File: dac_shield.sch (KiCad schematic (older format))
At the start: 26 parts, among them P1 V+, P2 GND, P3 V-, P4 Out, P5 GND, U1 LM741, U2 TCA0372

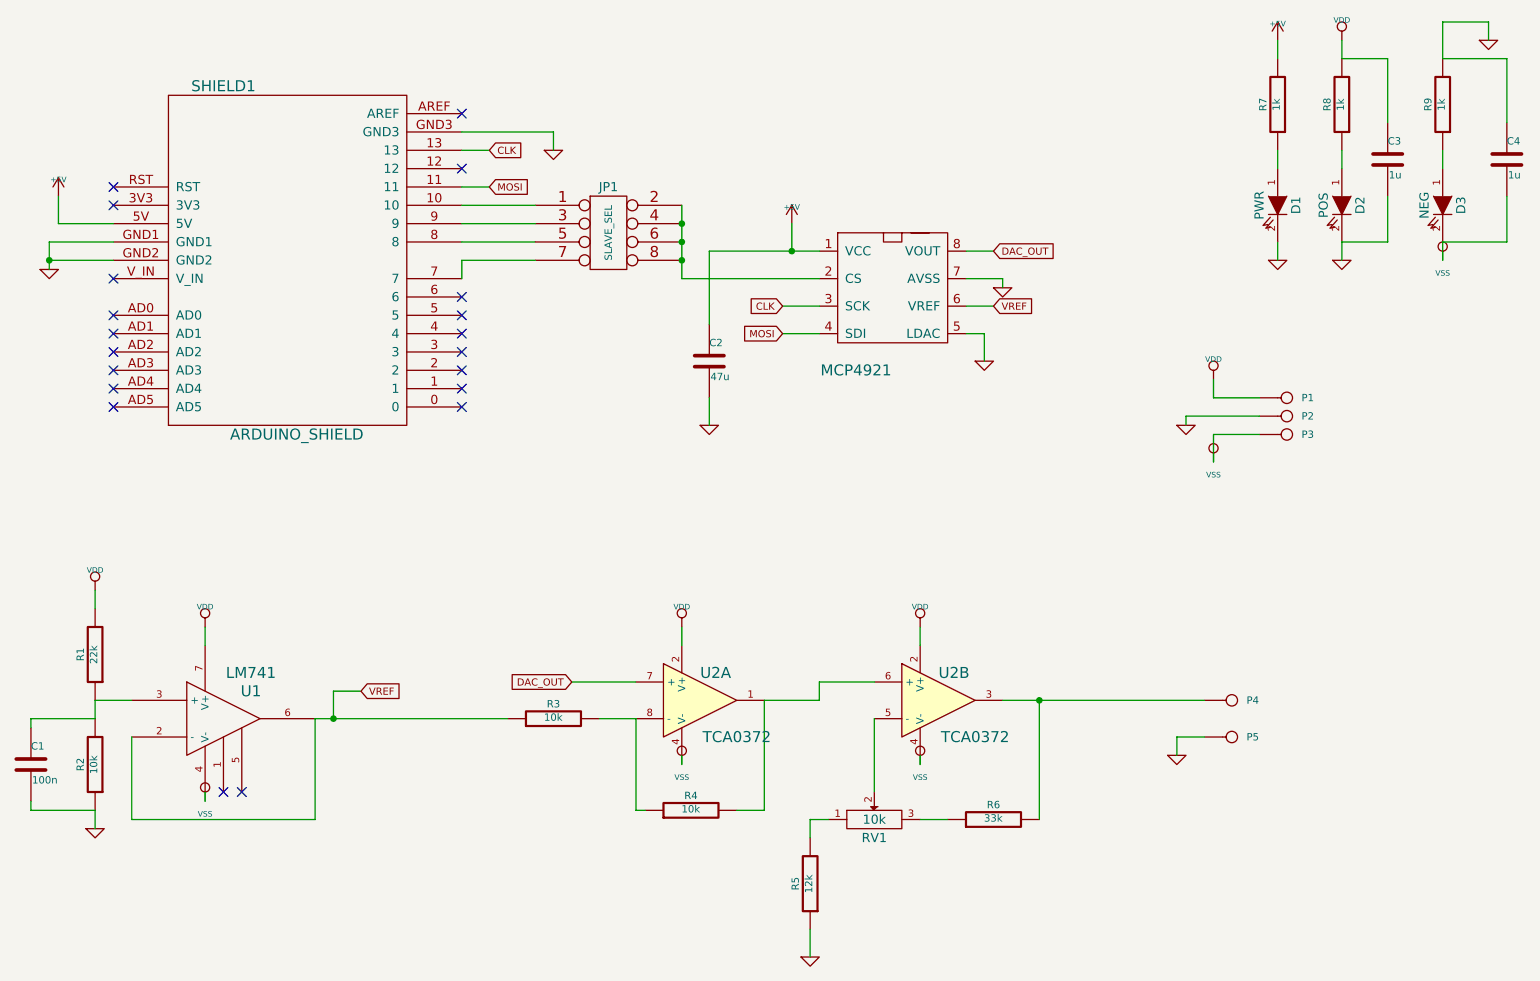
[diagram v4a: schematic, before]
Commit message: Fixed problem with MCP4921 now showing up
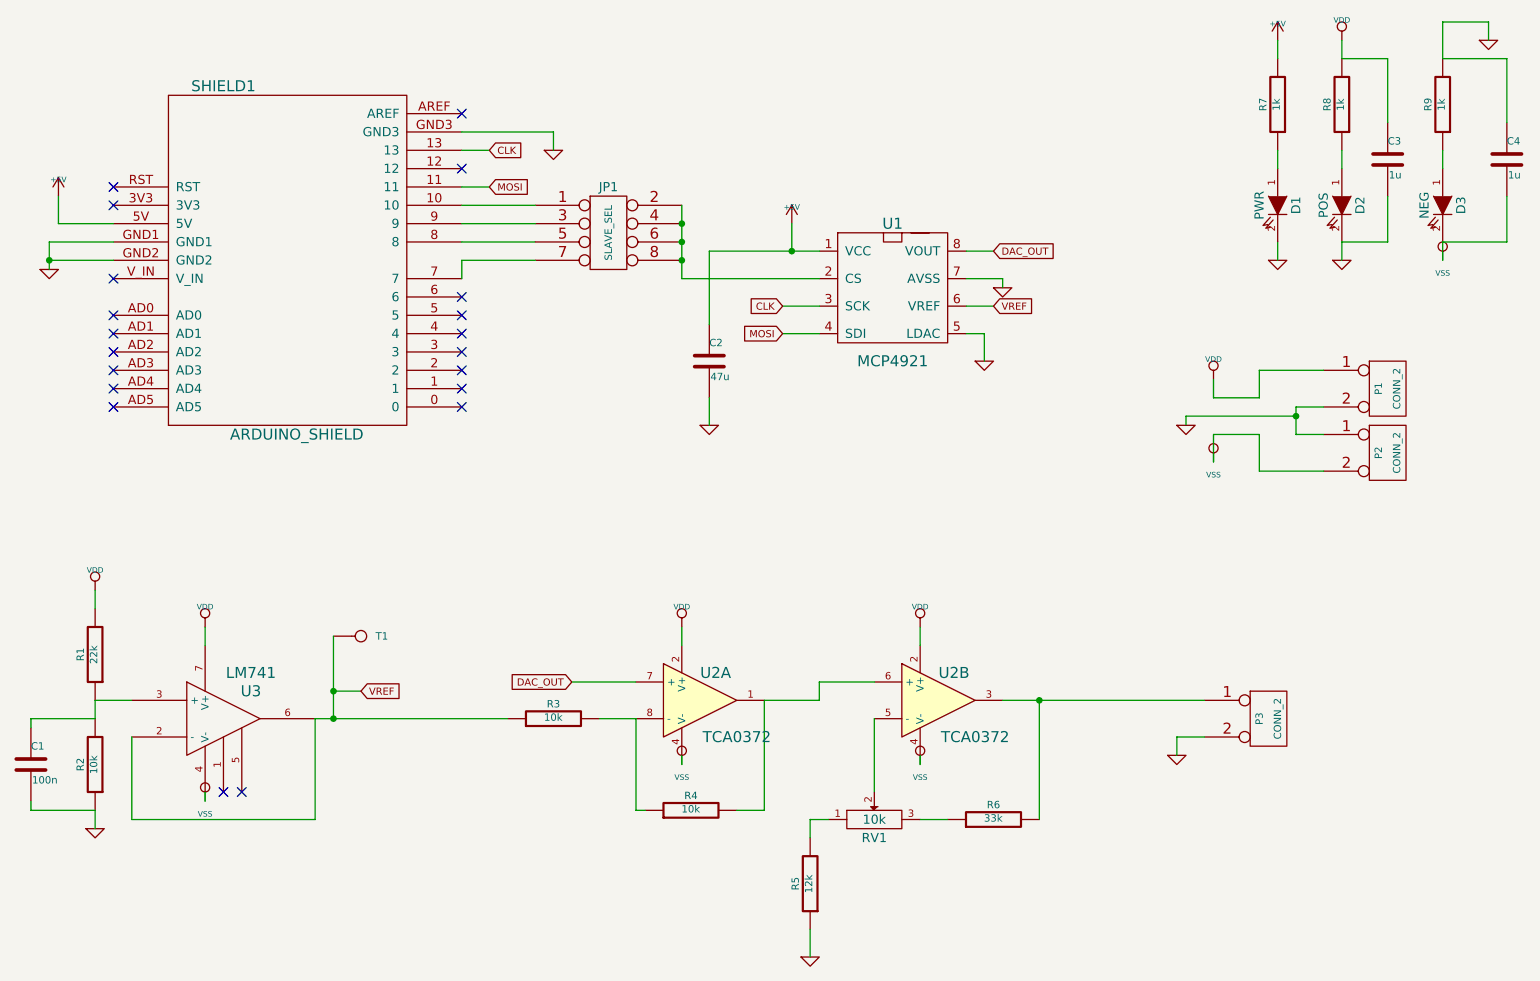
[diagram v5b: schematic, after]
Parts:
- removed P1: V+, symbol CONN_1
- removed P2, P5: GND, symbol CONN_1
- removed P3: V-, symbol CONN_1
- removed P4: Out, symbol CONN_1
- added P1, P2, P3: CONN_2, symbol CONN_2
- added T1: VrefTest, symbol CONN_1
- added U1: MCP4921, symbol MCP4921
- renumbered U1 to U3
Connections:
- net +5V: now also U1.1 (VCC)
- net CLK: now also U1.3 (SCK)
- net DAC_OUT: now also U1.8 (VOUT)
- net GND: now also P1.2 (PM), P2.1 (P1), P3.2 (PM), U1.5 (LDAC), U1.7 (AVSS)
- net MOSI: now also U1.4 (SDI)
- net VDD: now also P1.1 (P1)
- net VREF: now also T1.1, U1.6 (VREF)
- net VSS: now also P2.2 (PM)
- net at JP1.2, JP1.4, JP1.6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: now also U1.2 (CS)
- net at R6.2, U2.3: now also P3.1 (P1)
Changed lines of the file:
@@
 Sheet 1 1
 Title "Power DAC Shield"
-Date "23 jul 2013"
+Date "11 aug 2013"
 Rev ""
 Comp "Visgence Inc."
@@
 	1    0    0    -1
 $EndComp
-$Comp
-L MCP4921 #U01
-U 1 1 51E2FDD6
-P 5750 2300
-F 0 "#U01" H 5750 2650 60  0001 C CNN
-F 1 "MCP4921" H 5550 1850 60  0000 C CNN
-F 2 "" H 5750 2300 60  0000 C CNN
-F 3 "" H 5750 2300 60  0000 C CNN
-	1    5750 2300
-	1    0    0    -1
-$EndComp
 Text GLabel 3550 1550 2    39   Input ~ 0
 CLK
@@
 Connection ~ 4600 1950
 $Comp
-L +5V #PWR02
+L +5V #PWR01
 U 1 1 51E300D3
 P 1200 1800
-F 0 "#PWR02" H 1200 1890 20  0001 C CNN
+F 0 "#PWR01" H 1200 1890 20  0001 C CNN
 F 1 "+5V" H 1200 1890 30  0000 C CNN
 F 2 "" H 1200 1800 60  0000 C CNN
@@
 $EndComp
 $Comp
-L +5V #PWR03
+L +5V #PWR02
 U 1 1 51E300EF
 P 5200 1950
-F 0 "#PWR03" H 5200 2040 20  0001 C CNN
+F 0 "#PWR02" H 5200 2040 20  0001 C CNN
 F 1 "+5V" H 5200 2040 30  0000 C CNN
 F 2 "" H 5200 1950 60  0000 C CNN
@@
 	5200 2100 5200 1950
 $Comp
-L GND #PWR04
+L GND #PWR03
 U 1 1 51E30124
 P 3900 1550
-F 0 "#PWR04" H 3900 1550 30  0001 C CNN
+F 0 "#PWR03" H 3900 1550 30  0001 C CNN
 F 1 "GND" H 3900 1480 30  0001 C CNN
 F 2 "" H 3900 1550 60  0000 C CNN
@@
 	3900 1450 3900 1550
 $Comp
-L GND #PWR05
+L GND #PWR04
 U 1 1 51E3017A
 P 1150 2200
-F 0 "#PWR05" H 1150 2200 30  0001 C CNN
+F 0 "#PWR04" H 1150 2200 30  0001 C CNN
 F 1 "GND" H 1150 2130 30  0001 C CNN
 F 2 "" H 1150 2200 60  0000 C CNN
@@
 $EndComp
 $Comp
-L GND #PWR06
+L GND #PWR05
 U 1 1 51E30180
 P 6350 2300
-F 0 "#PWR06" H 6350 2300 30  0001 C CNN
+F 0 "#PWR05" H 6350 2300 30  0001 C CNN
 F 1 "GND" H 6350 2230 30  0001 C CNN
 F 2 "" H 6350 2300 60  0000 C CNN
@@
 $EndComp
 $Comp
-L VSS #PWR07
+L VSS #PWR06
 U 1 1 51E3066F
 P 5900 4900
-F 0 "#PWR07" H 5900 4900 30  0001 C CNN
+F 0 "#PWR06" H 5900 4900 30  0001 C CNN
 F 1 "VSS" H 5900 4830 30  0000 C CNN
 F 2 "" H 5900 4900 60  0000 C CNN
@@
 $EndComp
 $Comp
-L VDD #PWR08
+L VDD #PWR07
 U 1 1 51E3067E
 P 5900 4150
-F 0 "#PWR08" H 5900 4250 30  0001 C CNN
+F 0 "#PWR07" H 5900 4250 30  0001 C CNN
 F 1 "VDD" H 5900 4260 30  0000 C CNN
 F 2 "" H 5900 4150 60  0000 C CNN
@@
 $EndComp
 $Comp
-L VDD #PWR09
+L VDD #PWR08
 U 1 1 51E3068B
 P 4600 4150
-F 0 "#PWR09" H 4600 4250 30  0001 C CNN
+F 0 "#PWR08" H 4600 4250 30  0001 C CNN
 F 1 "VDD" H 4600 4260 30  0000 C CNN
 F 2 "" H 4600 4150 60  0000 C CNN
@@
 $EndComp
 $Comp
-L VSS #PWR010
+L VSS #PWR09
 U 1 1 51E30691
 P 4600 4900
-F 0 "#PWR010" H 4600 4900 30  0001 C CNN
+F 0 "#PWR09" H 4600 4900 30  0001 C CNN
 F 1 "VSS" H 4600 4830 30  0000 C CNN
 F 2 "" H 4600 4900 60  0000 C CNN
@@
 	5300 5200 5400 5200
 $Comp
-L GND #PWR011
+L GND #PWR010
 U 1 1 51E307ED
 P 5300 5950
-F 0 "#PWR011" H 5300 5950 30  0001 C CNN
+F 0 "#PWR010" H 5300 5950 30  0001 C CNN
 F 1 "GND" H 5300 5880 30  0001 C CNN
 F 2 "" H 5300 5950 60  0000 C CNN
@@
 DAC_OUT
 $Comp
-L LM741 U1
+L LM741 U3
 U 1 1 51E30A12
 P 2100 4650
-F 0 "U1" H 2250 4800 60  0000 C CNN
+F 0 "U3" H 2250 4800 60  0000 C CNN
 F 1 "LM741" H 2250 4900 60  0000 C CNN
 F 2 "" H 2100 4650 60  0000 C CNN
@@
 	1600 5200 1600 4750
 $Comp
-L VSS #PWR012
+L VSS #PWR011
 U 1 1 51E30A90
 P 2000 5100
-F 0 "#PWR012" H 2000 5100 30  0001 C CNN
+F 0 "#PWR011" H 2000 5100 30  0001 C CNN
 F 1 "VSS" H 2000 5030 30  0000 C CNN
 F 2 "" H 2000 5100 60  0000 C CNN
@@
 	2000 5050 2000 5100
 $Comp
-L VDD #PWR013
+L VDD #PWR012
 U 1 1 51E30AC8
 P 2000 4150
-F 0 "#PWR013" H 2000 4250 30  0001 C CNN
+F 0 "#PWR012" H 2000 4250 30  0001 C CNN
 F 1 "VDD" H 2000 4260 30  0000 C CNN
 F 2 "" H 2000 4150 60  0000 C CNN
@@
 $EndComp
 $Comp
-L VDD #PWR014
+L VDD #PWR013
 U 1 1 51E30B13
 P 1400 3950
-F 0 "#PWR014" H 1400 4050 30  0001 C CNN
+F 0 "#PWR013" H 1400 4050 30  0001 C CNN
 F 1 "VDD" H 1400 4060 30  0000 C CNN
 F 2 "" H 1400 3950 60  0000 C CNN
@@
 $EndComp
 $Comp
-L GND #PWR015
+L GND #PWR014
 U 1 1 51E30B25
 P 1400 5250
-F 0 "#PWR015" H 1400 5250 30  0001 C CNN
+F 0 "#PWR014" H 1400 5250 30  0001 C CNN
 F 1 "GND" H 1400 5180 30  0001 C CNN
 F 2 "" H 1400 5250 60  0000 C CNN
@@
 	2850 4500 2700 4500
 Wire Wire Line
-	2700 4500 2700 4650
+	2700 4200 2700 4650
 Connection ~ 2700 4650
 Text GLabel 6300 2400 2    39   Input ~ 0
@@
 	1200 1950 1200 1800
 $Comp
-L VDD #PWR016
+L VDD #PWR015
 U 1 1 51E30D84
 P 7500 2800
-F 0 "#PWR016" H 7500 2900 30  0001 C CNN
+F 0 "#PWR015" H 7500 2900 30  0001 C CNN
 F 1 "VDD" H 7500 2910 30  0000 C CNN
 F 2 "" H 7500 2800 60  0000 C CNN
@@
 	7500 2900 7500 2800
 $Comp
-L VSS #PWR017
+L VSS #PWR016
 U 1 1 51E30DC8
 P 7500 3250
-F 0 "#PWR017" H 7500 3250 30  0001 C CNN
+F 0 "#PWR016" H 7500 3250 30  0001 C CNN
 F 1 "VSS" H 7500 3180 30  0000 C CNN
 F 2 "" H 7500 3250 60  0000 C CNN
@@
 	7500 3100 7500 3250
 $Comp
-L GND #PWR018
+L GND #PWR017
 U 1 1 51E30E0E
 P 7350 3050
-F 0 "#PWR018" H 7350 3050 30  0001 C CNN
+F 0 "#PWR017" H 7350 3050 30  0001 C CNN
 F 1 "GND" H 7350 2980 30  0001 C CNN
 F 2 "" H 7350 3050 60  0000 C CNN
@@
 	7350 3050 7350 3000
 Wire Wire Line
-	7350 3000 7750 3000
+	7350 3000 7950 3000
 Connection ~ 6550 4550
 $Comp
-L GND #PWR019
+L GND #PWR018
 U 1 1 51E30EF3
 P 7300 4850
-F 0 "#PWR019" H 7300 4850 30  0001 C CNN
+F 0 "#PWR018" H 7300 4850 30  0001 C CNN
 F 1 "GND" H 7300 4780 30  0001 C CNN
 F 2 "" H 7300 4850 60  0000 C CNN
@@
 Connection ~ 5200 2100
 $Comp
-L GND #PWR020
+L GND #PWR019
 U 1 1 51E82617
 P 4750 3050
-F 0 "#PWR020" H 4750 3050 30  0001 C CNN
+F 0 "#PWR019" H 4750 3050 30  0001 C CNN
 F 1 "GND" H 4750 2980 30  0001 C CNN
 F 2 "" H 4750 3050 60  0000 C CNN
@@
 	4750 2900 4750 3050
 $Comp
-L +5V #PWR021
+L +5V #PWR020
 U 1 1 51E8266A
 P 7850 950
-F 0 "#PWR021" H 7850 1040 20  0001 C CNN
+F 0 "#PWR020" H 7850 1040 20  0001 C CNN
 F 1 "+5V" H 7850 1040 30  0000 C CNN
 F 2 "" H 7850 950 60  0000 C CNN
@@
 $EndComp
 $Comp
-L GND #PWR022
+L GND #PWR021
 U 1 1 51E8267F
 P 7850 2150
-F 0 "#PWR022" H 7850 2150 30  0001 C CNN
+F 0 "#PWR021" H 7850 2150 30  0001 C CNN
 F 1 "GND" H 7850 2080 30  0001 C CNN
 F 2 "" H 7850 2150 60  0000 C CNN
@@
 	7850 950  7850 1050
 $Comp
-L VDD #PWR023
+L VDD #PWR022
 U 1 1 51E827A2
 P 8200 950
-F 0 "#PWR023" H 8200 1050 30  0001 C CNN
+F 0 "#PWR022" H 8200 1050 30  0001 C CNN
 F 1 "VDD" H 8200 1060 30  0000 C CNN
 F 2 "" H 8200 950 60  0000 C CNN
@@
 	8200 1550 8200 1650
 $Comp
-L GND #PWR024
+L GND #PWR023
 U 1 1 51E82857
 P 8200 2150
-F 0 "#PWR024" H 8200 2150 30  0001 C CNN
+F 0 "#PWR023" H 8200 2150 30  0001 C CNN
 F 1 "GND" H 8200 2080 30  0001 C CNN
 F 2 "" H 8200 2150 60  0000 C CNN
@@
 	8200 2050 8200 2150
 $Comp
-L GND #PWR025
+L GND #PWR024
 U 1 1 51E828BA
 P 9000 950
-F 0 "#PWR025" H 9000 950 30  0001 C CNN
+F 0 "#PWR024" H 9000 950 30  0001 C CNN
 F 1 "GND" H 9000 880 30  0001 C CNN
 F 2 "" H 9000 950 60  0000 C CNN
@@
 	8750 1550 8750 1650
 $Comp
-L VSS #PWR026
+L VSS #PWR025
 U 1 1 51E829CC
 P 8750 2150
-F 0 "#PWR026" H 8750 2150 30  0001 C CNN
+F 0 "#PWR025" H 8750 2150 30  0001 C CNN
 F 1 "VSS" H 8750 2080 30  0000 C CNN
 F 2 "" H 8750 2150 60  0000 C CNN
@@
 	8450 2050 8200 2050
 $Comp
-L CONN_1 P1
-U 1 1 51E82EE8
-P 7900 2900
-F 0 "P1" H 7980 2900 40  0000 L CNN
-F 1 "V+" H 7900 2955 30  0001 C CNN
-F 2 "" H 7900 2900 60  0000 C CNN
-F 3 "" H 7900 2900 60  0000 C CNN
-	1    7900 2900
-	1    0    0    -1
-$EndComp
-$Comp
-L CONN_1 P2
-U 1 1 51E82EF5
-P 7900 3000
-F 0 "P2" H 7980 3000 40  0000 L CNN
-F 1 "GND" H 7900 3055 30  0001 C CNN
-F 2 "" H 7900 3000 60  0000 C CNN
-F 3 "" H 7900 3000 60  0000 C CNN
-	1    7900 3000
-	1    0    0    -1
-$EndComp
-$Comp
-L CONN_1 P3
-U 1 1 51E82EFB
-P 7900 3100
-F 0 "P3" H 7980 3100 40  0000 L CNN
-F 1 "V-" H 7900 3155 30  0001 C CNN
-F 2 "" H 7900 3100 60  0000 C CNN
-F 3 "" H 7900 3100 60  0000 C CNN
-	1    7900 3100
-	1    0    0    -1
-$EndComp
-$Comp
-L CONN_1 P4
-U 1 1 51E82F0B
-P 7600 4550
-F 0 "P4" H 7680 4550 40  0000 L CNN
-F 1 "Out" H 7600 4605 30  0001 C CNN
-F 2 "" H 7600 4550 60  0000 C CNN
-F 3 "" H 7600 4550 60  0000 C CNN
-	1    7600 4550
-	1    0    0    -1
-$EndComp
-$Comp
-L CONN_1 P5
-U 1 1 51E82F11
-P 7600 4750
-F 0 "P5" H 7680 4750 40  0000 L CNN
-F 1 "GND" H 7600 4805 30  0001 C CNN
-F 2 "" H 7600 4750 60  0000 C CNN
-F 3 "" H 7600 4750 60  0000 C CNN
-	1    7600 4750
-	1    0    0    -1
-$EndComp
-$Comp
-L GND #PWR027
+L GND #PWR026
 U 1 1 51EEC648
 P 6250 2700
-F 0 "#PWR027" H 6250 2700 30  0001 C CNN
+F 0 "#PWR026" H 6250 2700 30  0001 C CNN
 F 1 "GND" H 6250 2630 30  0001 C CNN
 F 2 "" H 6250 2700 60  0000 C CNN
@@
 NoConn ~ 2100 5050
 NoConn ~ 2200 5050
+$Comp
+L CONN_2 P1
+U 1 1 5207C384
+P 8450 2850
+F 0 "P1" V 8400 2850 40  0000 C CNN
+F 1 "CONN_2" V 8500 2850 40  0000 C CNN
+F 2 "" H 8450 2850 60  0000 C CNN
+F 3 "" H 8450 2850 60  0000 C CNN
+	1    8450 2850
+	1    0    0    -1
+$EndComp
+$Comp
+L CONN_2 P2
+U 1 1 5207C393
+P 8450 3200
+F 0 "P2" V 8400 3200 40  0000 C CNN
+F 1 "CONN_2" V 8500 3200 40  0000 C CNN
+F 2 "" H 8450 3200 60  0000 C CNN
+F 3 "" H 8450 3200 60  0000 C CNN
+	1    8450 3200
+	1    0    0    -1
+$EndComp
+$Comp
+L CONN_2 P3
+U 1 1 5207C3A2
+P 7800 4650
+F 0 "P3" V 7750 4650 40  0000 C CNN
+F 1 "CONN_2" V 7850 4650 40  0000 C CNN
+F 2 "" H 7800 4650 60  0000 C CNN
+F 3 "" H 7800 4650 60  0000 C CNN
+	1    7800 4650
+	1    0    0    -1
+$EndComp
+Wire Wire Line
+	7750 2900 7750 2750
+Wire Wire Line
+	7750 2750 8100 2750
+Wire Wire Line
+	7950 2950 7950 3100
+Wire Wire Line
+	7950 2950 8100 2950
+Wire Wire Line
+	7750 3100 7750 3300
+Wire Wire Line
+	7750 3300 8100 3300
+Wire Wire Line
+	7950 3100 8100 3100
+Connection ~ 7950 3000
+$Comp
+L CONN_1 T1
+U 1 1 5207C58D
+P 2850 4200
+F 0 "T1" H 2930 4200 40  0000 L CNN
+F 1 "VrefTest" H 2850 4255 30  0001 C CNN
+F 2 "" H 2850 4200 60  0000 C CNN
+F 3 "" H 2850 4200 60  0000 C CNN
+	1    2850 4200
+	1    0    0    -1
+$EndComp
+Connection ~ 2700 4500
+$Comp
+L MCP4921 U1
+U 1 1 5207D003
+P 5750 2300
+F 0 "U1" H 5750 2650 60  0000 C CNN
+F 1 "MCP4921" H 5750 1900 60  0000 C CNN
+F 2 "" H 5750 2300 60  0000 C CNN
+F 3 "" H 5750 2300 60  0000 C CNN
+	1    5750 2300
+	1    0    0    -1
+$EndComp
 $EndSCHEMATC

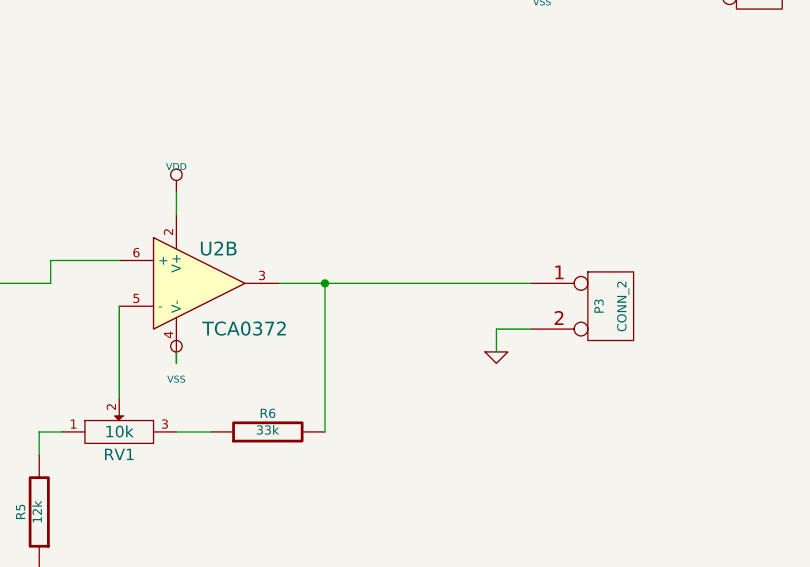
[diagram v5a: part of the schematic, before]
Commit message: Added fuse to output
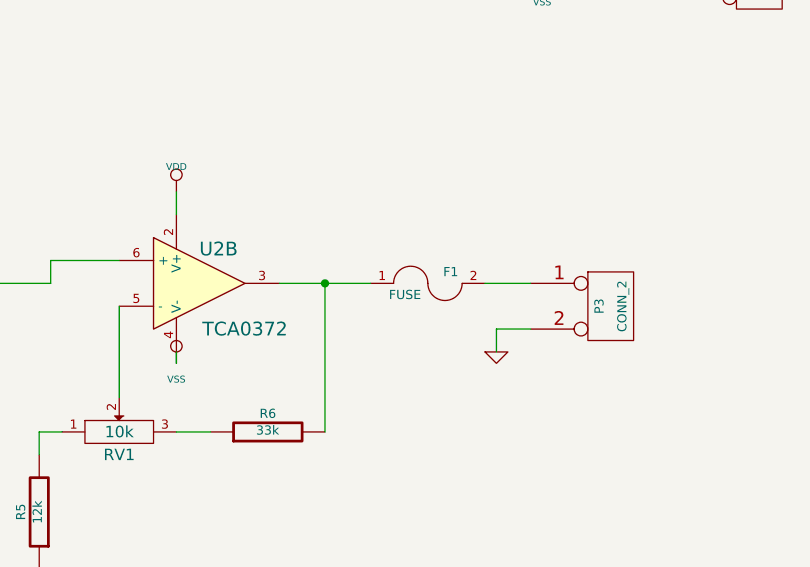
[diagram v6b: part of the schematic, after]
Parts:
- added F1: FUSE, ~, symbol FUSE
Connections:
- net at R6.2, U2.3: now also F1.1; no longer P3.1 (P1)
- new net: F1.2, P3.1 (P1)
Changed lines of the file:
@@
 Sheet 1 1
 Title "Power DAC Shield"
-Date "11 aug 2013"
+Date "21 sep 2013"
 Rev ""
 Comp "Visgence Inc."
@@
 Wire Wire Line
 	6550 5200 6550 4550
-Wire Wire Line
-	6350 4550 7450 4550
 $Comp
 L R R5
@@
 	1    0    0    -1
 $EndComp
+$Comp
+L FUSE F1
+U 1 1 523DF665
+P 7000 4550
+F 0 "F1" H 7100 4600 40  0000 C CNN
+F 1 "FUSE" H 6900 4500 40  0000 C CNN
+F 2 "~" H 7000 4550 60  0000 C CNN
+F 3 "~" H 7000 4550 60  0000 C CNN
+	1    7000 4550
+	1    0    0    -1
+$EndComp
+Wire Wire Line
+	7450 4550 7250 4550
+Wire Wire Line
+	6750 4550 6350 4550
 $EndSCHEMATC

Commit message: Made rev4 changes
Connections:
- net at RV1.1: now also R6.1; no longer R5.2
- net at RV1.3: now also R5.2; no longer R6.1
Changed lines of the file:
@@
 Sheet 1 1
 Title "Power DAC Shield"
-Date "21 sep 2013"
+Date "23 jul 2014"
 Rev ""
 Comp "Visgence Inc."
@@
 F 3 "~" H 5650 5200 60  0000 C CNN
 	1    5650 5200
-	1    0    0    -1
+	-1   0    0    -1
 $EndComp
 $Comp
